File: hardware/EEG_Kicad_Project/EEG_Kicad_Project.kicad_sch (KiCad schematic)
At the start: 0 parts

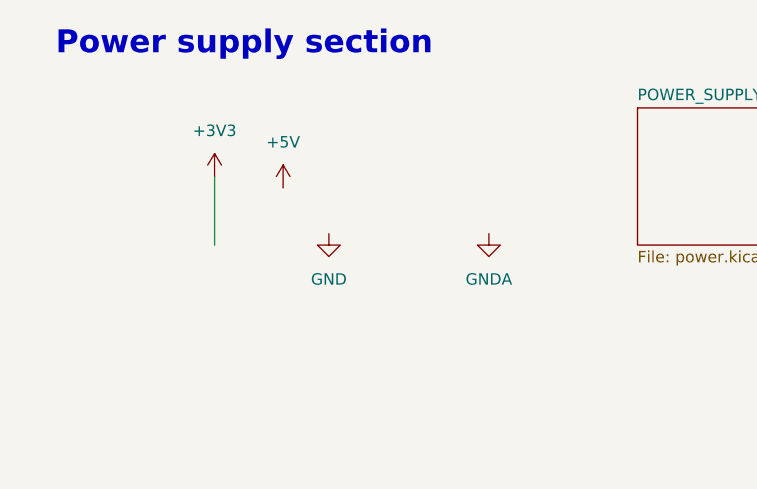
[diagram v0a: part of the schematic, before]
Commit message: Add USB galvanic isolation barrier for patient safety
Adds a USB-C receptacle -> ESD protection -> ADuM3160 isolator ->
isolated TMU3-0511 DC-DC chain, separating the STM32/ADS1299/analog
supply (now fully isolated) from the non-isolated USB-connector side.
Closes the previously-floating USB_OTG_FS_DP/DM pins on the STM32,
adds CC1/CC2 pulldowns and VBUS decoupling on the new receptacle, and
fixes ADuM3160 VBUS2 tie per datasheet. Verified via kicad-happy: no
ERC regressions, isolation barrier confirmed intact (no net bridges
GND_PRI/+5V_PRI with the isolated GNDA/+5V/+3V3 domain).

Co-Authored-By: Claude Sonnet 5 <noreply@anthropic.com>
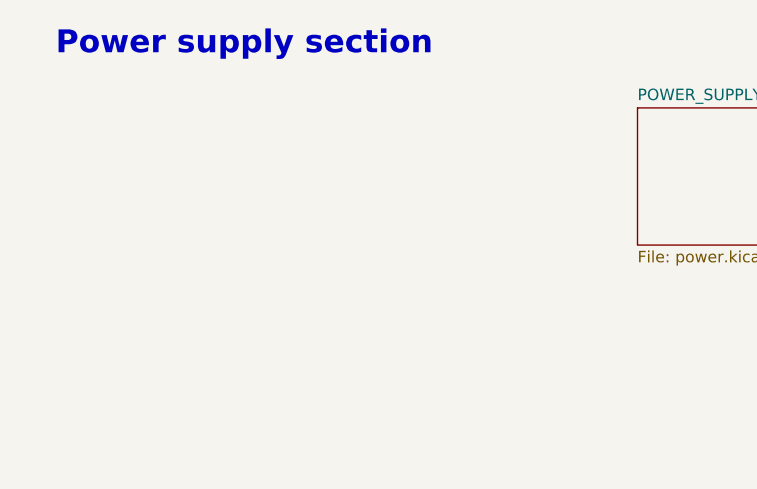
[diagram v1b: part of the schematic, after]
